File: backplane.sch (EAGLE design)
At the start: 44 parts, among them J1 L717HDE15PD4CH4R, J10 5013310807, J11 5013310807, J12 5013310807, J13 5013310807, J14 5013311007, J15 5013311007, J16 5013311007, J17 5013311007, J18 5013311007, J19 5013311007, J2 1054301102, J20 5013311007, J21 5013311007, J22 5013311007, J23 5013311007, J24 SEAM-40-03.0-S-06-2-A-K-TR, J3 5011902017, J4 5013310807, J5 5013310807, J6 5013310807, J7 5013310807, J8 5013310807, J9 5013310807, U1 AM26LV32EIPWR, U10 AM26LV32EIPWR, U2 AM26LV32EIPWR, U3 AM26LV32EIPWR, U4 AM26LV32EIPWR, U5 AM26LV32EIPWR, U6 AM26LV32EIPWR, U7 AM26LV32EIPWR, U8 AM26LV32EIPWR, U9 AM26LV32EIPWR

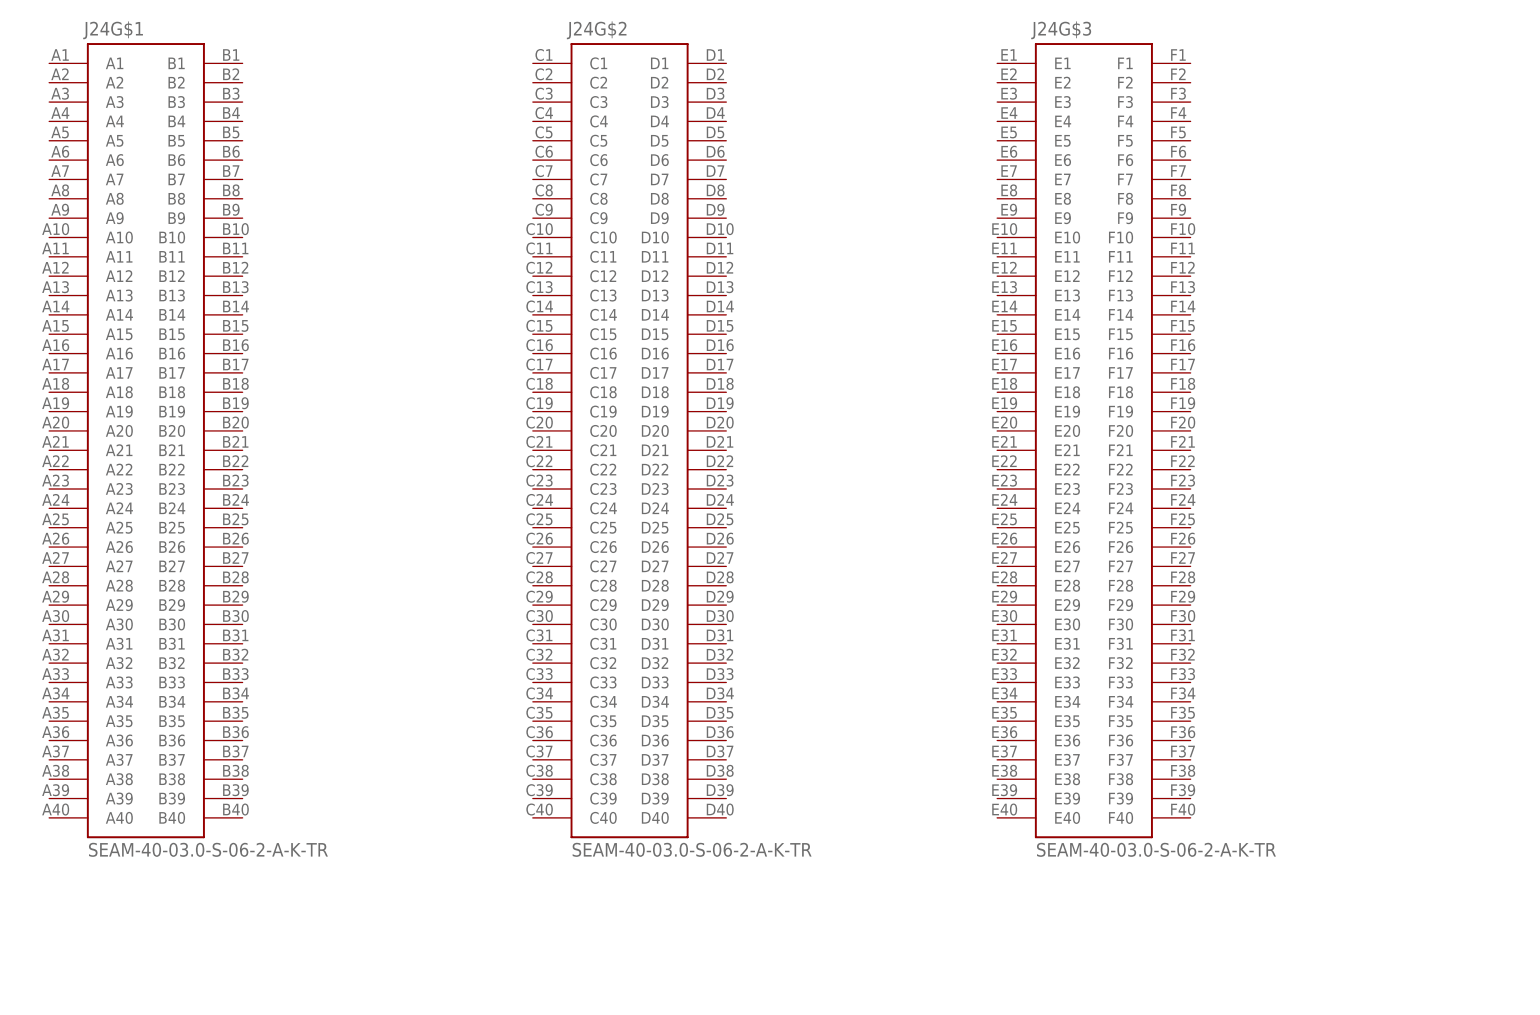
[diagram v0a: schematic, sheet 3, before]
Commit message: Started routing Encoder/AMC Connectors
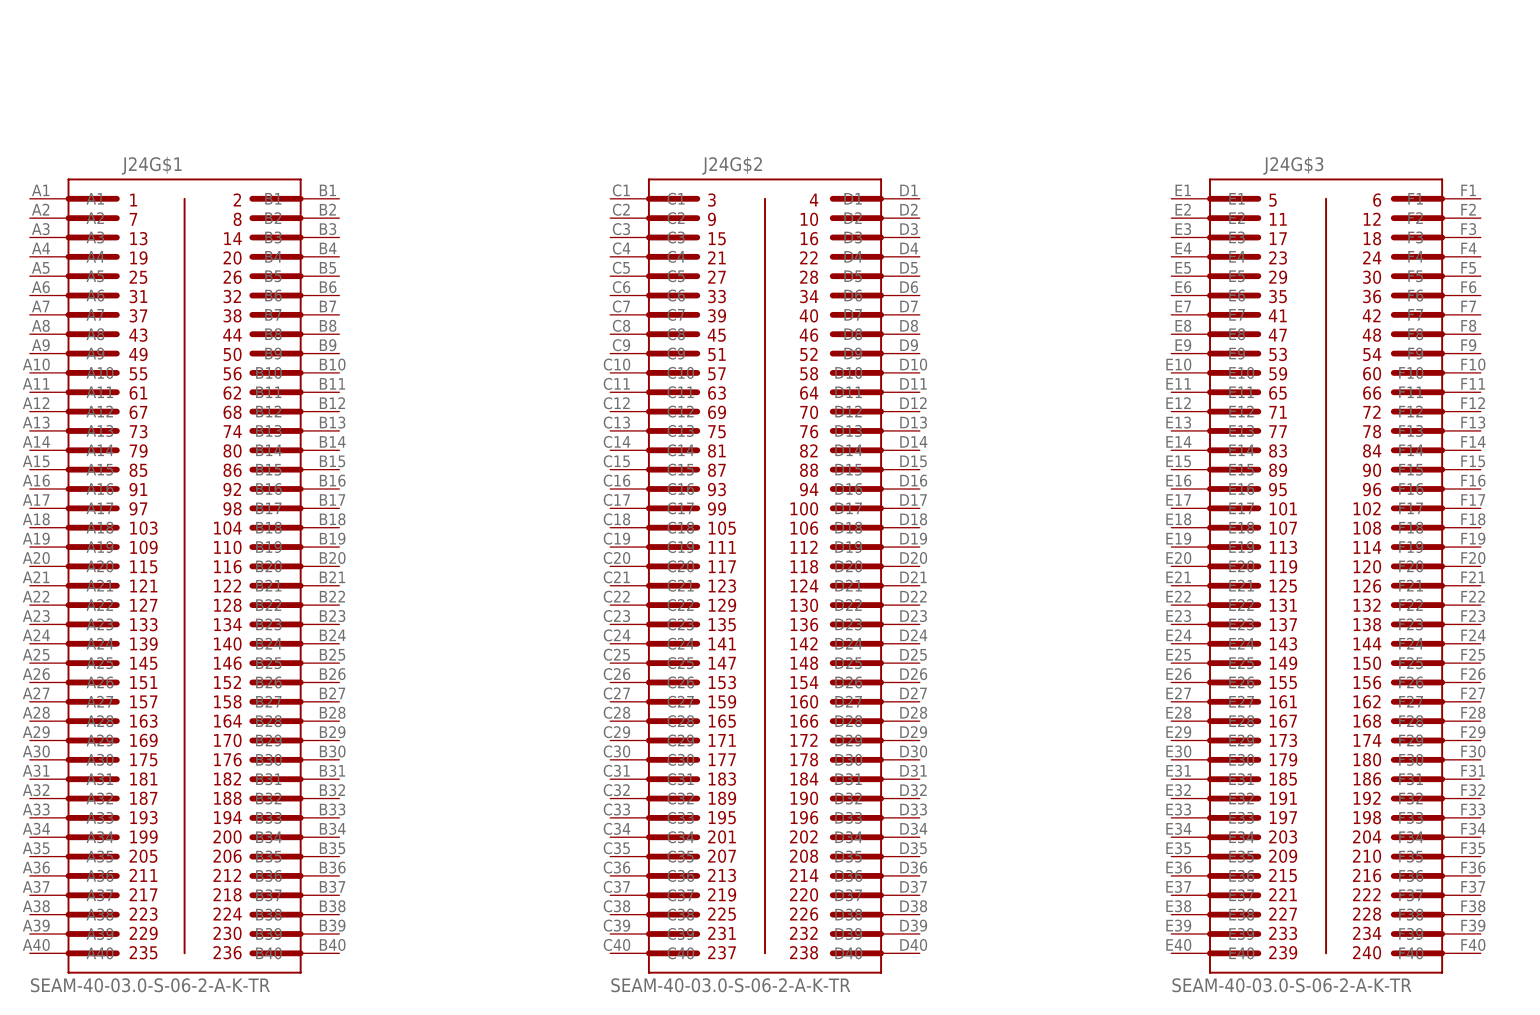
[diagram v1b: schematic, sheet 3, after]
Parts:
- added J25: 5055670271, sbrio_backplane:5055670271
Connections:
- new net 5V: J14.2, J15.2, J16.2, J17.2, J18.2, J19.2, J20.2, J21.2, J22.2, J23.2
- new net AGND: J10.8, J11.8, J12.8, J13.8, J4.8, J5.8, J6.8, J7.8, J8.8, J9.8
- new net ANA1: J13.7
- new net ANA10: J4.7
- new net ANA2: J8.7
- new net ANA3: J12.7
- new net ANA4: J7.7
- new net ANA5: J11.7
- new net ANA6: J6.7
- new net ANA7: J10.7
- new net ANA8: J5.7
- new net ANA9: J9.7
- new net A_M10_N: J14.9
- new net A_M10_P: J14.10
- new net A_M1_N: J23.9
- new net A_M1_P: J23.10
- new net A_M2_N: J18.9
- new net A_M2_P: J18.10
- new net A_M3_N: J22.9
- new net A_M3_P: J22.10
- new net A_M4_N: J17.9
- new net A_M4_P: J17.10
- new net A_M5_N: J21.9
- new net A_M5_P: J21.10
- new net A_M6_N: J16.9
- new net A_M6_P: J16.10
- new net A_M7_N: J20.9
- new net A_M7_P: J20.10
- new net A_M8_N: J15.9
- new net A_M8_P: J15.10
- new net A_M9_N: J19.9
- new net A_M9_P: J19.10
- new net B_M10_N: J14.7
- new net B_M10_P: J14.8
- new net B_M1_N: J23.7
- new net B_M1_P: J23.8
- new net B_M2_N: J18.7
- new net B_M2_P: J18.8
- new net B_M3_N: J22.7
- new net B_M3_P: J22.8
- new net B_M4_N: J17.7
- new net B_M4_P: J17.8
- new net B_M5_N: J21.7
- new net B_M5_P: J21.8
- new net B_M6_N: J16.7
- new net B_M6_P: J16.8
- new net B_M7_N: J20.7
- new net B_M7_P: J20.8
- new net B_M8_N: J15.7
- new net B_M8_P: J15.8
- new net B_M9_N: J19.7
- new net B_M9_P: J19.8
- new net ESTP+: J10.5, J11.5, J12.5, J13.5, J4.5, J5.5, J6.5, J7.5, J8.5, J9.5
- new net ESTP-: J10.6, J11.6, J12.6, J13.6, J4.6, J5.6, J6.6, J7.6, J8.6, J9.6
- new net GND: J10.10, J10.9, J11.10, J11.9, J12.10, J12.9, J13.10, J13.9, J14.1, J14.11, J14.12, J15.1, J15.11, J15.12, J16.1, J16.11, J16.12, J17.1, J17.11, J17.12, J18.1, J18.11, J18.12, J19.1, J19.11, J19.12, J20.1, J20.11, J20.12, J21.1, J21.11, J21.12, J22.1, J22.11, J22.12, J23.1, J23.11, J23.12, J4.10, J4.9, J5.10, J5.9, J6.10, J6.9, J7.10, J7.9, J8.10, J8.9, J9.10, J9.9
- new net MA_M10_N: J14.5, J4.2
- new net MA_M10_P: J14.6, J4.1
- new net MA_M1_N: J13.2, J23.5
- new net MA_M1_P: J13.1, J23.6
- new net MA_M2_N: J18.5, J8.2
- new net MA_M2_P: J18.6, J8.1
- new net MA_M3_N: J12.2, J22.5
- new net MA_M3_P: J12.1, J22.6
- new net MA_M4_N: J17.5, J7.2
- new net MA_M4_P: J17.6, J7.1
- new net MA_M5_N: J11.2, J21.5
- new net MA_M5_P: J11.1, J21.6
- new net MA_M6_N: J16.5, J6.2
- new net MA_M6_P: J16.6, J6.1
- new net MA_M7_N: J10.2, J20.5
- new net MA_M7_P: J10.1, J20.6
- new net MA_M8_N: J15.5, J5.2
- new net MA_M8_P: J15.6, J5.1
- new net MA_M9_N: J19.5, J9.2
- new net MA_M9_P: J19.6, J9.1
- new net SLO_M10_N: J14.3, J4.4
- new net SLO_M10_P: J14.4, J4.3
- new net SLO_M1_N: J13.4, J23.3
- new net SLO_M1_P: J13.3, J23.4
- new net SLO_M2_N: J18.3, J8.4
- new net SLO_M2_P: J18.4, J8.3
- new net SLO_M3_N: J12.4, J22.3
- new net SLO_M3_P: J12.3, J22.4
- new net SLO_M4_N: J17.3, J7.4
- new net SLO_M4_P: J17.4, J7.3
- new net SLO_M5_N: J11.4, J21.3
- new net SLO_M5_P: J11.3, J21.4
- new net SLO_M6_N: J16.3, J6.4
- new net SLO_M6_P: J16.4, J6.3
- new net SLO_M7_N: J10.4, J20.3
- new net SLO_M7_P: J10.3, J20.4
- new net SLO_M8_N: J15.3, J5.4
- new net SLO_M8_P: J15.4, J5.3
- new net SLO_M9_N: J19.3, J9.4
- new net SLO_M9_P: J19.4, J9.3
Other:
- note added: "MAKE ALL DIFFERENTIAL PAIRS THE RIGHT NET CLASS"

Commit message: encoder/amc connectors mostly routed
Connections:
- new net 3V3: U1.VCC, U10.VCC, U2.VCC, U3.VCC, U4.VCC, U5.VCC, U6.VCC, U7.VCC, U8.VCC, U9.VCC
- new net A_M1: RN10.4, U10.3Y
- new net A_M10: RN1.4, U1.3Y
- new net A_M2: RN5.4, U5.3Y
- new net A_M3: RN9.4, U9.3Y
- new net A_M4: RN4.4, U4.3Y
- new net A_M5: RN8.4, U8.3Y
- new net A_M6: RN3.4, U3.3Y
- new net A_M7: RN7.4, U7.3Y
- new net A_M8: RN2.4, U2.3Y
- new net A_M9: RN6.4, U6.3Y
- new net B_M1: RN10.3, U10.4Y
- new net B_M10: RN1.3, U1.4Y
- new net B_M2: RN5.3, U5.4Y
- new net B_M3: RN9.3, U9.4Y
- new net B_M4: RN4.3, U4.4Y
- new net B_M5: RN8.3, U8.4Y
- new net B_M6: RN3.3, U3.4Y
- new net B_M7: RN7.3, U7.4Y
- new net B_M8: RN2.3, U2.4Y
- new net B_M9: RN6.3, U6.4Y
- new net MA_M1: RN10.2, U10.2Y
- new net MA_M10: RN1.2, U1.2Y
- new net MA_M2: RN5.2, U5.2Y
- new net MA_M3: RN9.2, U9.2Y
- new net MA_M4: RN4.2, U4.2Y
- new net MA_M5: RN8.2, U8.2Y
- new net MA_M6: RN3.2, U3.2Y
- new net MA_M7: RN7.2, U7.2Y
- new net MA_M8: RN2.2, U2.2Y
- new net MA_M9: RN6.2, U6.2Y
- new net N$1: RN9.5
- new net N$10: RN10.7
- new net N$108: U4.G
- new net N$11: RN10.8
- new net N$115: U3.!G
- new net N$12: RN8.7
- new net N$124: U3.G
- new net N$13: U10.G
- new net N$131: U2.!G
- new net N$14: RN8.8
- new net N$140: U2.G
- new net N$147: U1.!G
- new net N$15: RN7.5
- new net N$156: U1.G
- new net N$16: RN7.6
- new net N$17: RN7.7
- new net N$18: RN7.8
- new net N$19: RN6.5
- new net N$2: RN9.6
- new net N$20: RN6.6
- new net N$21: RN6.7
- new net N$22: RN6.8
- new net N$23: U9.!G
- new net N$24: RN5.5
- new net N$25: RN5.6
- new net N$26: RN5.7
- new net N$27: RN5.8
- new net N$28: RN4.5
- new net N$29: RN4.6
- new net N$3: RN9.7
- new net N$30: U9.G
- new net N$31: RN4.7
- new net N$32: RN4.8
- new net N$33: RN3.5
- new net N$34: RN3.6
- new net N$35: RN3.7
- new net N$36: RN3.8
- new net N$37: U8.!G
- new net N$38: RN2.5
- new net N$39: RN2.6
- new net N$4: U10.!G
- new net N$40: RN2.7
- new net N$41: RN2.8
- new net N$42: RN1.5
- new net N$43: RN1.6
- new net N$44: U8.G
- new net N$45: RN1.7
- new net N$46: RN1.8
- new net N$5: RN9.8
- new net N$51: U7.!G
- new net N$6: RN8.5
- new net N$60: U7.G
- new net N$67: U6.!G
- new net N$7: RN8.6
- new net N$76: U6.G
- new net N$8: RN10.5
- new net N$85: U5.!G
- new net N$9: RN10.6
- new net N$92: U5.G
- new net N$99: U4.!G
- new net SLO_M1: RN10.1, U10.1Y
- new net SLO_M10: RN1.1, U1.1Y
- new net SLO_M2: RN5.1, U5.1Y
- new net SLO_M3: RN9.1, U9.1Y
- new net SLO_M4: RN4.1, U4.1Y
- new net SLO_M5: RN8.1, U8.1Y
- new net SLO_M6: RN3.1, U3.1Y
- new net SLO_M7: RN7.1, U7.1Y
- new net SLO_M8: RN2.1, U2.1Y
- new net SLO_M9: RN6.1, U6.1Y
- net AGND: now also J3.10, J3.11, J3.14, J3.15, J3.18, J3.19, J3.2, J3.3, J3.6, J3.7
- net ANA1: now also J3.20
- net ANA10: now also J3.17
- net ANA2: now also J3.16
- net ANA3: now also J3.12
- net ANA4: now also J3.8
- net ANA5: now also J3.4
- net ANA6: now also J3.1
- net ANA7: now also J3.5
- net ANA8: now also J3.9
- net ANA9: now also J3.13
- net A_M10_N: now also U1.3B
- net A_M10_P: now also U1.3A
- net A_M1_N: now also U10.3B
- net A_M1_P: now also U10.3A
- net A_M2_N: now also U5.3B
- net A_M2_P: now also U5.3A
- net A_M3_N: now also U9.3B
- net A_M3_P: now also U9.3A
- net A_M4_N: now also U4.3B
- net A_M4_P: now also U4.3A
- net A_M5_N: now also U8.3B
- net A_M5_P: now also U8.3A
- net A_M6_N: now also U3.3B
- net A_M6_P: now also U3.3A
- net A_M7_N: now also U7.3B
- net A_M7_P: now also U7.3A
- net A_M8_N: now also U2.3B
- net A_M8_P: now also U2.3A
- net A_M9_N: now also U6.3B
- net A_M9_P: now also U6.3A
- net B_M10_N: now also U1.4B
- net B_M10_P: now also U1.4A
- net B_M1_N: now also U10.4B
- net B_M1_P: now also U10.4A
- net B_M2_N: now also U5.4B
- net B_M2_P: now also U5.4A
- net B_M3_N: now also U9.4B
- net B_M3_P: now also U9.4A
- net B_M4_N: now also U4.4B
- net B_M4_P: now also U4.4A
- net B_M5_N: now also U8.4B
- net B_M5_P: now also U8.4A
- net B_M6_N: now also U3.4B
- net B_M6_P: now also U3.4A
- net B_M7_N: now also U7.4B
- net B_M7_P: now also U7.4A
- net B_M8_N: now also U2.4B
- net B_M8_P: now also U2.4A
- net B_M9_N: now also U6.4B
- net B_M9_P: now also U6.4A
- net GND: now also J3.21, J3.22, U1.GND, U10.GND, U2.GND, U3.GND, U4.GND, U5.GND, U6.GND, U7.GND, U8.GND, U9.GND
- net MA_M10_N: now also U1.2B
- net MA_M10_P: now also U1.2A
- net MA_M1_N: now also U10.2B
- net MA_M1_P: now also U10.2A
- net MA_M2_N: now also U5.2B
- net MA_M2_P: now also U5.2A
- net MA_M3_N: now also U9.2B
- net MA_M3_P: now also U9.2A
- net MA_M4_N: now also U4.2B
- net MA_M4_P: now also U4.2A
- net MA_M5_N: now also U8.2B
- net MA_M5_P: now also U8.2A
- net MA_M6_N: now also U3.2B
- net MA_M6_P: now also U3.2A
- net MA_M7_N: now also U7.2B
- net MA_M7_P: now also U7.2A
- net MA_M8_N: now also U2.2B
- net MA_M8_P: now also U2.2A
- net MA_M9_N: now also U6.2B
- net MA_M9_P: now also U6.2A
- net SLO_M10_N: now also U1.1B
- net SLO_M10_P: now also U1.1A
- net SLO_M1_N: now also U10.1B
- net SLO_M1_P: now also U10.1A
- net SLO_M2_N: now also U5.1B
- net SLO_M2_P: now also U5.1A
- net SLO_M3_N: now also U9.1B
- net SLO_M3_P: now also U9.1A
- net SLO_M4_N: now also U4.1B
- net SLO_M4_P: now also U4.1A
- net SLO_M5_N: now also U8.1B
- net SLO_M5_P: now also U8.1A
- net SLO_M6_N: now also U3.1B
- net SLO_M6_P: now also U3.1A
- net SLO_M7_N: now also U7.1B
- net SLO_M7_P: now also U7.1A
- net SLO_M8_N: now also U2.1B
- net SLO_M8_P: now also U2.1A
- net SLO_M9_N: now also U6.1B
- net SLO_M9_P: now also U6.1A
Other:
- note added: "ADD 0.1uF Capacitors to all"
- note removed: "MAKE ALL DIFFERENTIAL PAIRS THE RIGHT NET CLASS"
